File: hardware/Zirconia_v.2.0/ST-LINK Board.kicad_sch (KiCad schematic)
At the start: 8 parts, among them J2 Conn_01x04, J4 BD125-10-A-0305-0580-L-B, U12 STLINK-V3MOS, U7 MCP73831T-2ACI/OT

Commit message: update
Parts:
- J2: value Conn_01x04 -> AE-FT234X
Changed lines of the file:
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@@
 		(on_board yes)
 		(dnp no)
-		(fields_autoplaced yes)
 		(property "Reference" "J2"
-			(at 161.29 101.5999 0)
+			(at 154.686 92.964 0)
 			(effects
 				(font
@@
 			)
 		)
-		(property "Value" "Conn_01x04"
-			(at 161.29 104.1399 0)
+		(property "Value" "AE-FT234X"
+			(at 151.13 95.504 0)
 			(effects
 				(font

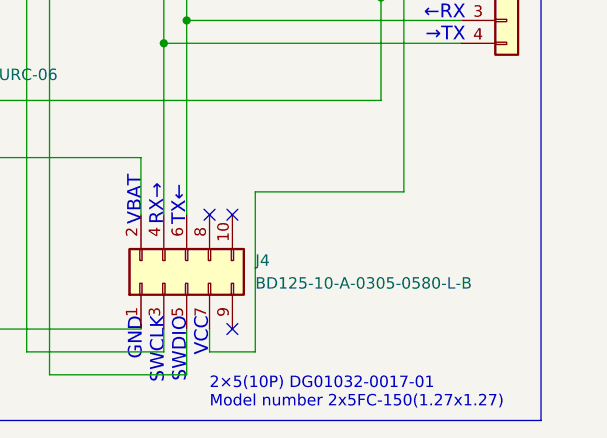
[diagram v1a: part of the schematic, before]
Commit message: JLCPCBパーツ反映
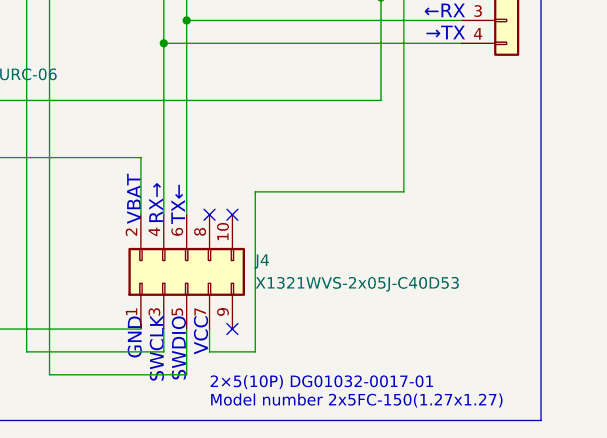
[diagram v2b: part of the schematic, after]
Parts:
- J4: value BD125-10-A-0305-0580-L-B -> X1321WVS-2x05J-C40D53; LCSC Part # (none) -> X1321WVS-2x05J-C40D53
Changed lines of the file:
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@@
 			)
 		)
-		(property "Value" "BD125-10-A-0305-0580-L-B"
+		(property "Value" "X1321WVS-2x05J-C40D53"
 			(at 130.81 133.35 90)
 			(effects
@@
 			(at 123.19 133.35 0)
 			(effects
+				(font
+					(size 1.27 1.27)
+				)
+				(hide yes)
+			)
+		)
+		(property "LCSC Part #" "X1321WVS-2x05J-C40D53"
+			(at 123.19 133.35 0)
+			(effects
